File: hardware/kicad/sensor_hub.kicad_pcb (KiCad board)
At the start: 2 copper layers, 100 x 100 mm, 66 parts, among them J1 1-1478035-0, J10 Wago-Relay2, J11 Spare-GPIO, J2 Wago-DS18B20, J3 Wago-DHT22, J4 Wago-PIR, J5 Wago-GP16, J6 Wago-GP17, J7 Wago-Relay1, J8 Phoenix-EC4pin, J9 Phoenix-Power, K1 G2RL-1-E DC5, K2 G2RL-1-E DC5, Q1 BC817-40, Q2 BSS84PXUMA1, Q3 BC817-40, U1 Pico WH, U2 ADS1115IDGSR, U4 AD8603ARTZ-R2, U5 AP2112K-3.3TRG1, U6 VEML7700-TT

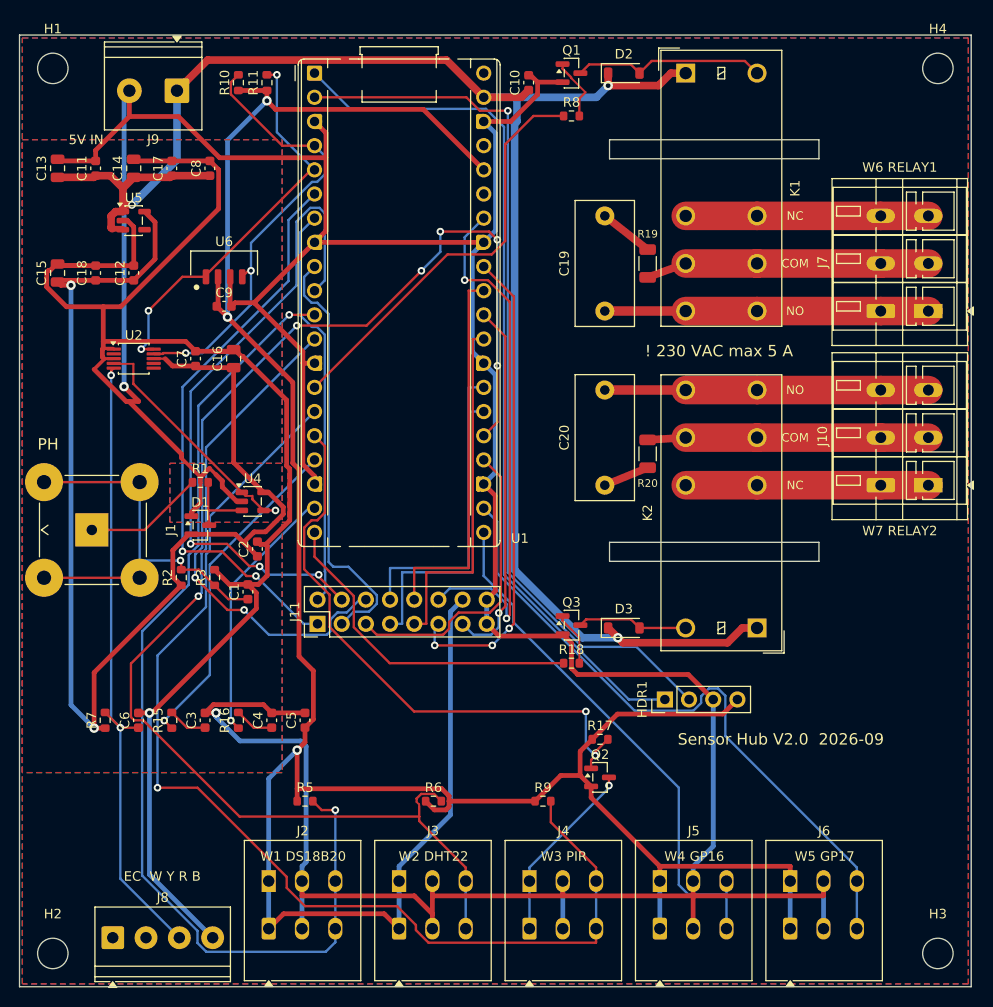
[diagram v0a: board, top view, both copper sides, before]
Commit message: hardware: Wago push-in for J8/J9, exposed pH guard, JLCPCB SMD assembly files
- J8 (EC) / J9 (5V in): Phoenix screw -> Wago 2601-1104 / 2601-1102, same
  family as J2-J6; power block moved down 3.5 mm, J2-J6 row shifted 0.6 mm
- pH guard: top-side guard copper exposed (mask opening = fill - 0.1 mm,
  footprint silkscreen kept masked); CLAUDE.md analog-zone rules updated
- route_pcb finish rerunnable (clears its own pours)
- jlc_export.py + fab/: gerbers.zip, bom_jlc.csv, cpl_jlc.csv (39 SMD parts,
  17 LCSC lines, DNP and THT excluded); bom.csv gains an lcsc column
- U4 order code fixed: AD8603AUJZ (ARTZ does not exist)

Co-Authored-By: Claude Opus 5.5 <noreply@anthropic.com>
Claude-Session: https://claude.ai/code/session_01PDHupfXBxwLmo1MxXKJEdB
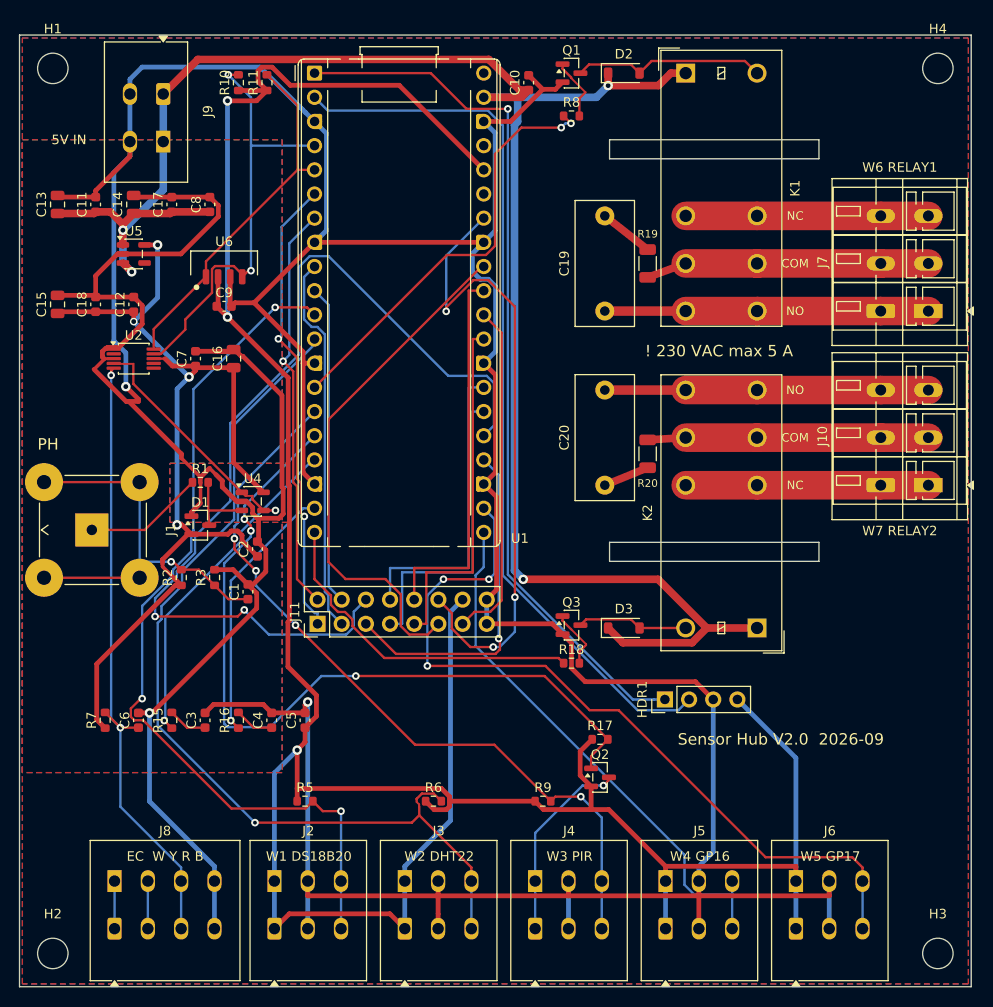
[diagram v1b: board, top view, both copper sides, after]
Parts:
- J8: value Phoenix-EC4pin -> Wago-EC4pin; footprint TerminalBlock_Phoenix:TerminalBlock_Phoenix_PT-1,5-4-3.5-H_1x04_P3.50mm_Horizontal -> TerminalBlock_WAGO:TerminalBlock_WAGO_2601-1104_1x04_P3.50mm_Horizontal
- J9: value Phoenix-Power -> Wago-Power; footprint TerminalBlock_Phoenix:TerminalBlock_Phoenix_PT-1,5-2-5.0-H_1x02_P5.00mm_Horizontal -> TerminalBlock_WAGO:TerminalBlock_WAGO_2601-1102_1x02_P3.50mm_Horizontal
- U4: value AD8603ARTZ-R2 -> AD8603AUJZ
- moved C11 3.80 mm to (48.0, 57.8)
- moved C13 3.80 mm to (44.0, 57.8)
- moved C14 3.80 mm to (52.0, 57.8)
- moved C17 3.80 mm to (56.0, 57.8)
- moved C8 3.80 mm to (60.0, 57.8)
- moved U5 3.50 mm to (52.0, 63.0)
- moved C12 3.30 mm to (52.0, 68.3)
- moved C15 3.30 mm to (44.0, 68.3)
- moved C18 3.30 mm to (48.0, 68.3)
- moved J9 1.48 mm to (55.1, 46.2)
- moved J8 0.97 mm to (50.0, 133.9)
- moved J4 0.60 mm to (94.2, 133.9)
- moved J5 0.60 mm to (107.9, 133.9)
- moved J2 0.60 mm to (66.8, 133.9)
- moved J3 0.60 mm to (80.5, 133.9)
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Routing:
- net /PIR_OUT: track 117.0 -> 81.2 mm, vias 1 -> 4
- net /GP7: track 69.3 -> 33.6 mm, vias 3 -> 0
- net /3V3_ANA: track 132.4 -> 106.0 mm, vias 2 -> 4
- net /GND_ANA: track 188.9 -> 165.2 mm
- net /PIR_EN_N: track 62.4 -> 84.0 mm, vias 2 -> 3
- net /VSYS: track 182.8 -> 200.8 mm, vias 3 -> 4
- net /ONEWIRE: track 109.4 -> 93.0 mm, vias 2 -> 3
- net /W5_SIG: track 69.3 -> 83.7 mm, vias 0 -> 3
- net /3V3_DIG: track 283.1 -> 296.2 mm
- net /GP4: track 60.6 -> 48.6 mm
- net /GP28: track 56.3 -> 67.3 mm, vias 2 -> 3
- net /GND: track 378.5 -> 372.9 mm
- net unconnected-(J8-Pin_2-Pad2): track 0.00 -> 5.00 mm
- net unconnected-(J8-Pin_1-Pad1): track 0.00 -> 5.00 mm
- net /GP6: track 44.9 -> 40.0 mm
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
